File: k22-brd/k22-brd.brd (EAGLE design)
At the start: 22.9 x 63.5 mm, 34 parts, among them J1 61302011121, J2 61302011121, J3 CORTEX_DEBUG_PTH

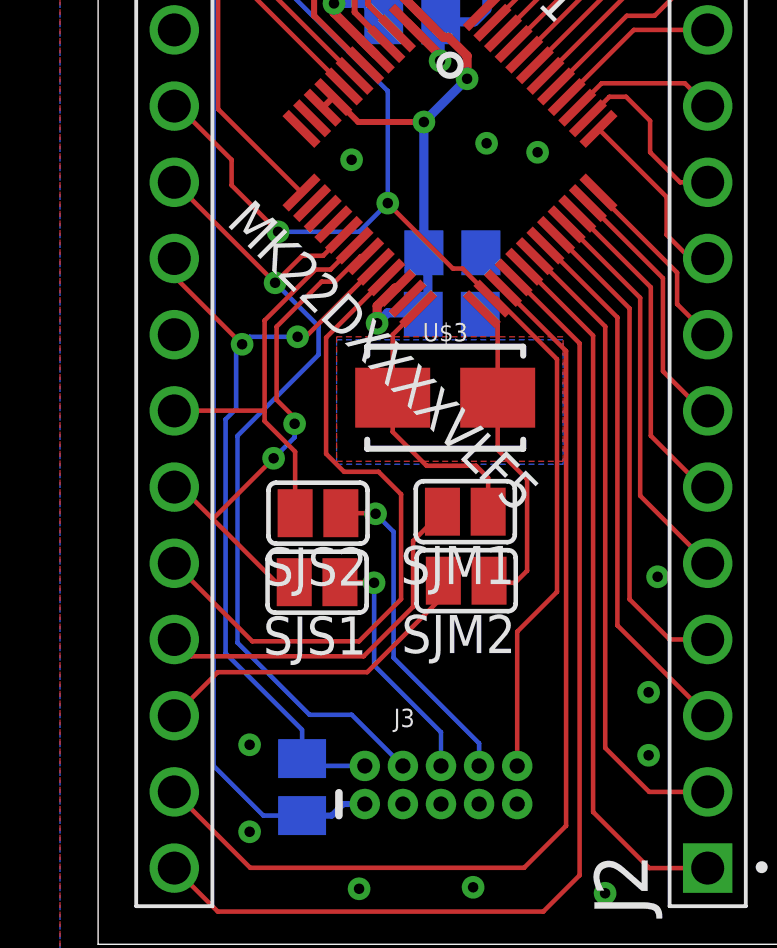
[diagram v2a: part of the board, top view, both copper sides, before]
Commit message: Improved routing
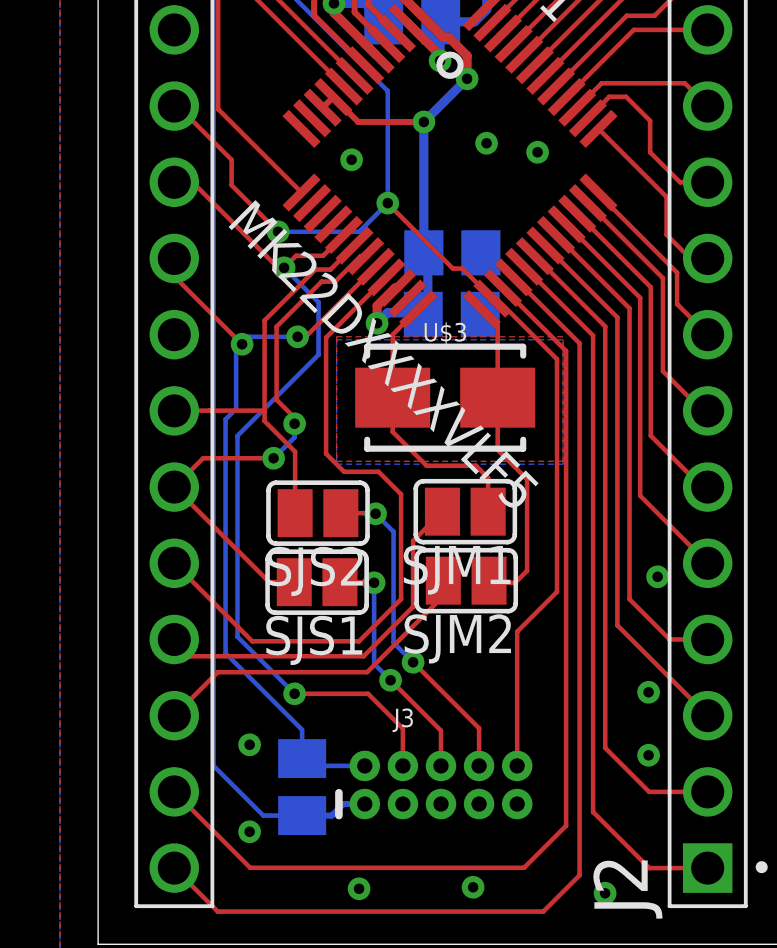
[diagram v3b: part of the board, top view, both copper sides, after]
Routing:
- net UART_TX: track 17.0 -> 17.9 mm
- net SWD_CLK: track 28.6 -> 29.2 mm, vias 1 -> 2
- net N$4: vias 1 -> 2
- net N$3: vias 1 -> 2
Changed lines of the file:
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@@
 <contactref element="J1" pad="11"/>
 <wire x1="8.194465625" y1="23.645125" x2="7.499340625" y2="22.95" width="0.1524" layer="1"/>
-<wire x1="7.499340625" y1="22.95" x2="6.8" y2="22.95" width="0.1524" layer="1"/>
-<wire x1="6.8" y1="22.95" x2="5.9" y2="22.05" width="0.1524" layer="1"/>
-<wire x1="5.9" y1="22.05" x2="2.55" y2="25.4" width="0.1524" layer="1"/>
-<wire x1="2.54" y1="25.4" x2="2.55" y2="25.4" width="0.1524" layer="1"/>
-<wire x1="10.16" y1="5.945" x2="8.455" y2="7.65" width="0.1524" layer="16"/>
+<wire x1="7.499340625" y1="22.95" x2="6.6" y2="22.95" width="0.1524" layer="1"/>
+<wire x1="6.6" y1="22.95" x2="6.2" y2="22.55" width="0.1524" layer="1"/>
+<wire x1="6.2" y1="22.55" x2="6" y2="22.55" width="0.1524" layer="1"/>
+<wire x1="6" y1="22.55" x2="3.15" y2="25.4" width="0.1524" layer="1"/>
+<wire x1="2.54" y1="25.4" x2="3.15" y2="25.4" width="0.1524" layer="1"/>
 <wire x1="4.6456" y1="16.9456" x2="7.35" y2="19.65" width="0.1524" layer="16"/>
-<wire x1="4.6456" y1="10.0544" x2="4.6456" y2="16.9456" width="0.1524" layer="16"/>
-<wire x1="7.35" y1="19.65" x2="7.35" y2="20.6" width="0.1524" layer="16"/>
-<wire x1="7.35" y1="20.6" x2="5.9" y2="22.05" width="0.1524" layer="16"/>
-<via x="5.9" y="22.05" extent="1-16" drill="0.35"/>
-<wire x1="8.455" y1="7.65" x2="7.05" y2="7.65" width="0.1524" layer="16"/>
-<wire x1="7.05" y1="7.65" x2="4.6456" y2="10.0544" width="0.1524" layer="16"/>
+<wire x1="4.6456" y1="10.2544" x2="4.6456" y2="16.9456" width="0.1524" layer="16"/>
+<wire x1="7.35" y1="19.65" x2="7.35" y2="21.4" width="0.1524" layer="16"/>
+<wire x1="7.35" y1="21.4" x2="6.2" y2="22.55" width="0.1524" layer="16"/>
+<via x="6.2" y="22.55" extent="1-16" drill="0.35"/>
+<wire x1="10.16" y1="5.945" x2="10.16" y2="7.19" width="0.1524" layer="1"/>
+<wire x1="9" y1="8.35" x2="6.55" y2="8.35" width="0.1524" layer="1"/>
+<via x="6.55" y="8.35" extent="1-16" drill="0.35"/>
+<wire x1="6.55" y1="8.35" x2="4.6456" y2="10.2544" width="0.1524" layer="16"/>
+<wire x1="10.16" y1="7.19" x2="9" y2="8.35" width="0.1524" layer="1"/>
 </signal>
 <signal name="UART_RX">
@@
 <wire x1="6.568" y1="14.37" x2="6.568" y2="16.42" width="0.1524" layer="1"/>
 <wire x1="6.568" y1="16.42" x2="5.55" y2="17.438" width="0.1524" layer="1"/>
-<wire x1="5.55" y1="17.788" x2="2.548" y2="17.788" width="0.1524" layer="1"/>
+<wire x1="5.55" y1="17.788" x2="3.7" y2="17.788" width="0.1524" layer="1"/>
+<wire x1="3.7" y1="17.788" x2="2.548" y2="17.788" width="0.1524" layer="1"/>
 <wire x1="2.548" y1="17.788" x2="2.54" y2="17.78" width="0.1524" layer="1"/>
 <wire x1="7.24801875" y1="22.491571875" x2="5.55" y2="20.793553125" width="0.1524" layer="1"/>
@@
 <contactref element="SJS1" pad="2"/>
 <contactref element="J1" pad="15"/>
-<wire x1="6.538" y1="12.07" x2="5.93" y2="12.07" width="0.1524" layer="1"/>
-<wire x1="2.76" y1="15.24" x2="2.54" y2="15.24" width="0.1524" layer="1"/>
-<wire x1="5.93" y1="12.07" x2="3.825" y2="14.175" width="0.1524" layer="1"/>
-<wire x1="3.825" y1="14.175" x2="2.76" y2="15.24" width="0.1524" layer="1"/>
-<wire x1="3.825" y1="14.175" x2="5.85" y2="16.2" width="0.1524" layer="1"/>
 <via x="5.85" y="16.2" extent="1-16" drill="0.35"/>
 <wire x1="6.55" y1="17.35" x2="6.55" y2="16.9" width="0.1524" layer="16"/>
@@
 <wire x1="6.55" y1="17.55" x2="5.95" y2="18.15" width="0.1524" layer="1"/>
 <wire x1="5.95" y1="20.586446875" x2="5.95" y2="18.15" width="0.1524" layer="1"/>
+<wire x1="3.5" y1="16.2" x2="2.54" y2="15.24" width="0.1524" layer="1"/>
+<wire x1="5.85" y1="16.2" x2="3.5" y2="16.2" width="0.1524" layer="1"/>
+<wire x1="5.71" y1="12.07" x2="2.54" y2="15.24" width="0.1524" layer="1"/>
+<wire x1="6.538" y1="12.07" x2="5.71" y2="12.07" width="0.1524" layer="1"/>
 </signal>
 <signal name="SWD_DIO">
@@
 <via x="9.25" y="14.35" extent="1-16" drill="0.35"/>
 <wire x1="9.25" y1="14.35" x2="9.85" y2="13.75" width="0.1524" layer="16"/>
-<wire x1="12.7" y1="6.7" x2="12.7" y2="5.945" width="0.1524" layer="16"/>
-<wire x1="9.85" y1="13.75" x2="9.85" y2="9.55" width="0.1524" layer="16"/>
-<wire x1="9.85" y1="9.55" x2="12.7" y2="6.7" width="0.1524" layer="16"/>
+<wire x1="9.85" y1="10.05" x2="9.85" y2="13.75" width="0.1524" layer="16"/>
+<wire x1="12.7" y1="5.945" x2="12.7" y2="7.2" width="0.1524" layer="1"/>
+<wire x1="12.7" y1="7.2" x2="10.5" y2="9.4" width="0.1524" layer="1"/>
+<via x="10.5" y="9.4" extent="1-16" drill="0.35"/>
+<wire x1="10.5" y1="9.4" x2="9.85" y2="10.05" width="0.1524" layer="16"/>
 </signal>
 <signal name="N$4">
@@
 <wire x1="9.18" y1="12.07" x2="9.2" y2="12.05" width="0.1524" layer="1"/>
 <via x="9.2" y="12.05" extent="1-16" drill="0.35"/>
-<wire x1="9.2" y1="12.05" x2="9.2" y2="9.3" width="0.1524" layer="16"/>
-<wire x1="11.43" y1="7.07" x2="11.43" y2="5.945" width="0.1524" layer="16"/>
-<wire x1="9.2" y1="9.3" x2="11.43" y2="7.07" width="0.1524" layer="16"/>
+<wire x1="11.43" y1="5.945" x2="11.43" y2="7.12" width="0.1524" layer="1"/>
+<wire x1="11.43" y1="7.12" x2="9.75" y2="8.8" width="0.1524" layer="1"/>
+<via x="9.75" y="8.8" extent="1-16" drill="0.35"/>
+<wire x1="9.2" y1="12.05" x2="9.2" y2="9.35" width="0.1524" layer="16"/>
+<wire x1="9.75" y1="8.8" x2="9.2" y2="9.35" width="0.1524" layer="16"/>
 </signal>
 <signal name="N$2">

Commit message: prezehleno
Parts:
- removed U$4: USBLC6-4SC6Y, vym0038_k22_misc:SOT23-6L
- added CU1: <1,10>u, rcl:C0805
- added U$5: USBLC6-2SC6, vym0038_k22_misc:SOT23-6L
- moved SJS2 7.67 mm to (12.7, 8.89), flipped to the bottom, turned to 90 degrees
- moved SJS1 4.27 mm to (10.2, 8.89), flipped to the bottom, turned to 90 degrees
- moved LU1 3.62 mm to (4.45, 54.9), turned to 90 degrees
- moved LU2 2.91 mm to (18.4, 54.9), turned to 90 degrees
- moved DV1 2.70 mm to (8.26, 46.0)
- moved CV2 2.59 mm to (11.7, 41.3), turned to 0 degrees
- moved DV2 2.32 mm to (5.71, 46.0)
- moved SJM1 2.13 mm to (10.2, 14.0), flipped to the bottom, turned to 270 degrees
- moved SJM2 1.90 mm to (12.7, 14.0), flipped to the bottom, turned to 270 degrees
- moved LED_3V3 1.87 mm to (16.2, 50.8), turned to 0 degrees
- moved RV1 1.70 mm to (16.5, 51.1), turned to 0 degrees
- moved SWR 1.50 mm to (6.99, 39.1)
- moved SWB 1.36 mm to (16.2, 39.1)
- moved CM4 0.95 mm to (11.4, 30.8)
- moved CV1 0.90 mm to (11.4, 51.1)
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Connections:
- net D+CON: now also U$5.3, U$5.4; no longer U$4.3
- net D-CON: now also U$5.1, U$5.6; no longer U$4.4
- net GND: now also CU1.1, U$5.2; no longer U$4.2
- net USB5V: now also CU1.2, J1.3; no longer J1.2
- net VBUSCON: now also U$5.5; no longer U$4.5
- net VIN: now also J1.2; no longer J1.3
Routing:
- net UART_RX: track 13.9 -> 23.0 mm, vias 0 -> 1
- net PTA4: track 22.5 -> 13.6 mm
- net N$3: track 11.0 -> 2.18 mm, vias 2 -> 0
- net GND: track 8.83 -> 15.3 mm, vias 13 -> 28
- net VBUSCON: track 16.6 -> 22.2 mm, vias 2 -> 3
- net N$4: track 8.17 -> 2.99 mm, vias 2 -> 0
- net D+CON: track 20.0 -> 24.9 mm, vias 0 -> 1
- net PTA19_OSC: track 10.8 -> 6.84 mm, vias 0 -> 1
- net VIN: track 7.10 -> 3.25 mm
- net PTA18: track 12.5 -> 9.55 mm, vias 0 -> 1
- net D-CON: track 20.1 -> 23.0 mm, vias 0 -> 4
- net PTA18_OSC: track 9.39 -> 6.84 mm, vias 0 -> 1
- net USB5V: track 31.6 -> 34.1 mm, vias 0 -> 1
- net UART_TX: track 17.9 -> 20.0 mm, vias 2 -> 1
- net RESET: track 44.1 -> 42.0 mm
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
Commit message: Nejake zmeny
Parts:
- moved DV1 0.32 mm to (7.94, 46.0)
- moved DV2 0.32 mm to (5.40, 46.0)
- moved CM2 0.32 mm to (11.4, 24.1)
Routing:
- net N$2: track 2.85 -> 3.92 mm
- net USB5V: track 34.1 -> 34.8 mm

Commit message: uprava routovani D+/-
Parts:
- moved U$5 0.32 mm to (11.4, 51.8)
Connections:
- net D+CON: now also U$5.1, U$5.6; no longer U$5.3, U$5.4
- net D-CON: now also U$5.3, U$5.4; no longer U$5.1, U$5.6
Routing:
- net D+CON: track 25.0 -> 22.5 mm
- net VBUSCON: track 22.3 -> 21.1 mm
- net GND: vias 28 -> 27

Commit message: jen detaily
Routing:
- net PTD4: track 16.1 -> 16.7 mm
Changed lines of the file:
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@@
 <via x="4.445" y="1.27" extent="1-16" drill="0.3"/>
 <via x="18.415" y="1.27" extent="1-16" drill="0.3"/>
-<via x="9.525" y="26.67" extent="1-16" drill="0.3"/>
+<via x="9.525" y="26.035" extent="1-16" drill="0.3"/>
 <via x="8.73125" y="20.6375" extent="1-16" drill="0.3"/>
 <wire x1="10.015784375" y1="21.438803125" x2="10.685975" y2="22.10899375" width="0.1524" layer="1"/>
@@
 <contactref element="J2" pad="17"/>
 <contactref element="SWB" pad="3"/>
-<wire x1="16.9825" y1="37.0025" x2="16.9925" y2="37.0025" width="0.1524" layer="1"/>
-<wire x1="13.55131875" y1="29.924084375" x2="16.9825" y2="33.355265625" width="0.1524" layer="1"/>
-<wire x1="16.9825" y1="33.355265625" x2="16.9825" y2="37.0025" width="0.1524" layer="1"/>
+<wire x1="13.55131875" y1="29.924084375" x2="17.78" y2="34.152765625" width="0.1524" layer="1"/>
+<wire x1="16.9925" y1="37.0025" x2="17.78" y2="36.215" width="0.1524" layer="1"/>
+<wire x1="17.78" y1="36.215" x2="17.78" y2="34.152765625" width="0.1524" layer="1"/>
 <wire x1="16.9925" y1="37.0025" x2="17.78" y2="37.79" width="0.1524" layer="1"/>
 <wire x1="17.78" y1="37.79" x2="17.78" y2="38.735" width="0.1524" layer="1"/>
@@
 <wire x1="10.4775" y1="26.3525" x2="10.4775" y2="24.1325" width="0.3048" layer="16"/>
 <wire x1="10.4775" y1="24.1325" x2="10.48" y2="24.13" width="0.3048" layer="16"/>
-<wire x1="12.7" y1="28.575" x2="11.7475" y2="27.6225" width="0.1524" layer="1"/>
-<wire x1="11.7475" y1="27.6225" x2="8.89" y2="27.6225" width="0.1524" layer="1"/>
-<wire x1="8.89" y1="27.6225" x2="8.482365625" y2="27.214865625" width="0.1524" layer="1"/>
+<wire x1="12.7" y1="28.575" x2="12.065" y2="27.94" width="0.1524" layer="1"/>
+<wire x1="12.065" y1="27.94" x2="9.2075" y2="27.94" width="0.1524" layer="1"/>
+<wire x1="9.2075" y1="27.94" x2="8.482365625" y2="27.214865625" width="0.1524" layer="1"/>
 <wire x1="4.1275" y1="32.0675" x2="3.175" y2="33.02" width="0.1524" layer="16"/>
 <wire x1="6.8" y1="4.29" x2="5.5525" y2="4.29" width="0.1524" layer="16"/>
